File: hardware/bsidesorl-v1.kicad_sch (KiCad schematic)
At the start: 36 parts, among them J1 SAO Connector, U1 CH32V003F4P6, U2 TPS61023DRLR

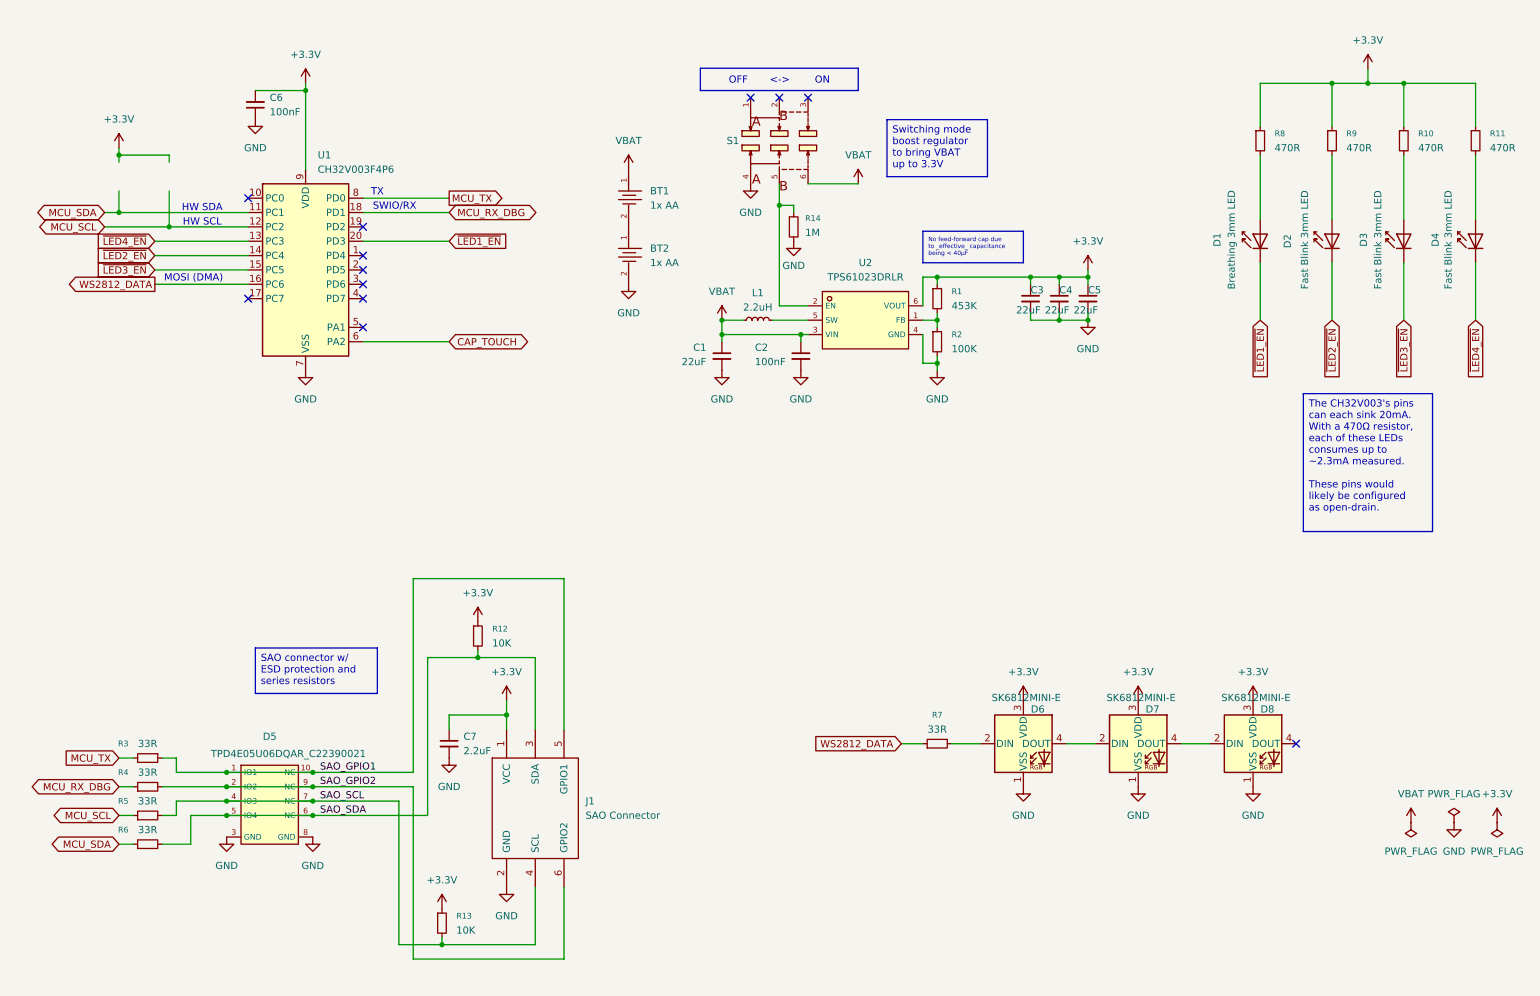
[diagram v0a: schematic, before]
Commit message: Final schematic, ready to order
* Switched from 2x AAs to 1x AAA
* Switched boost IC from TPS61023 to TPS61021A for lower VIN requirement due to single cell design change
* Added a second capacitive touch area just because
* Finalize back silkscreen
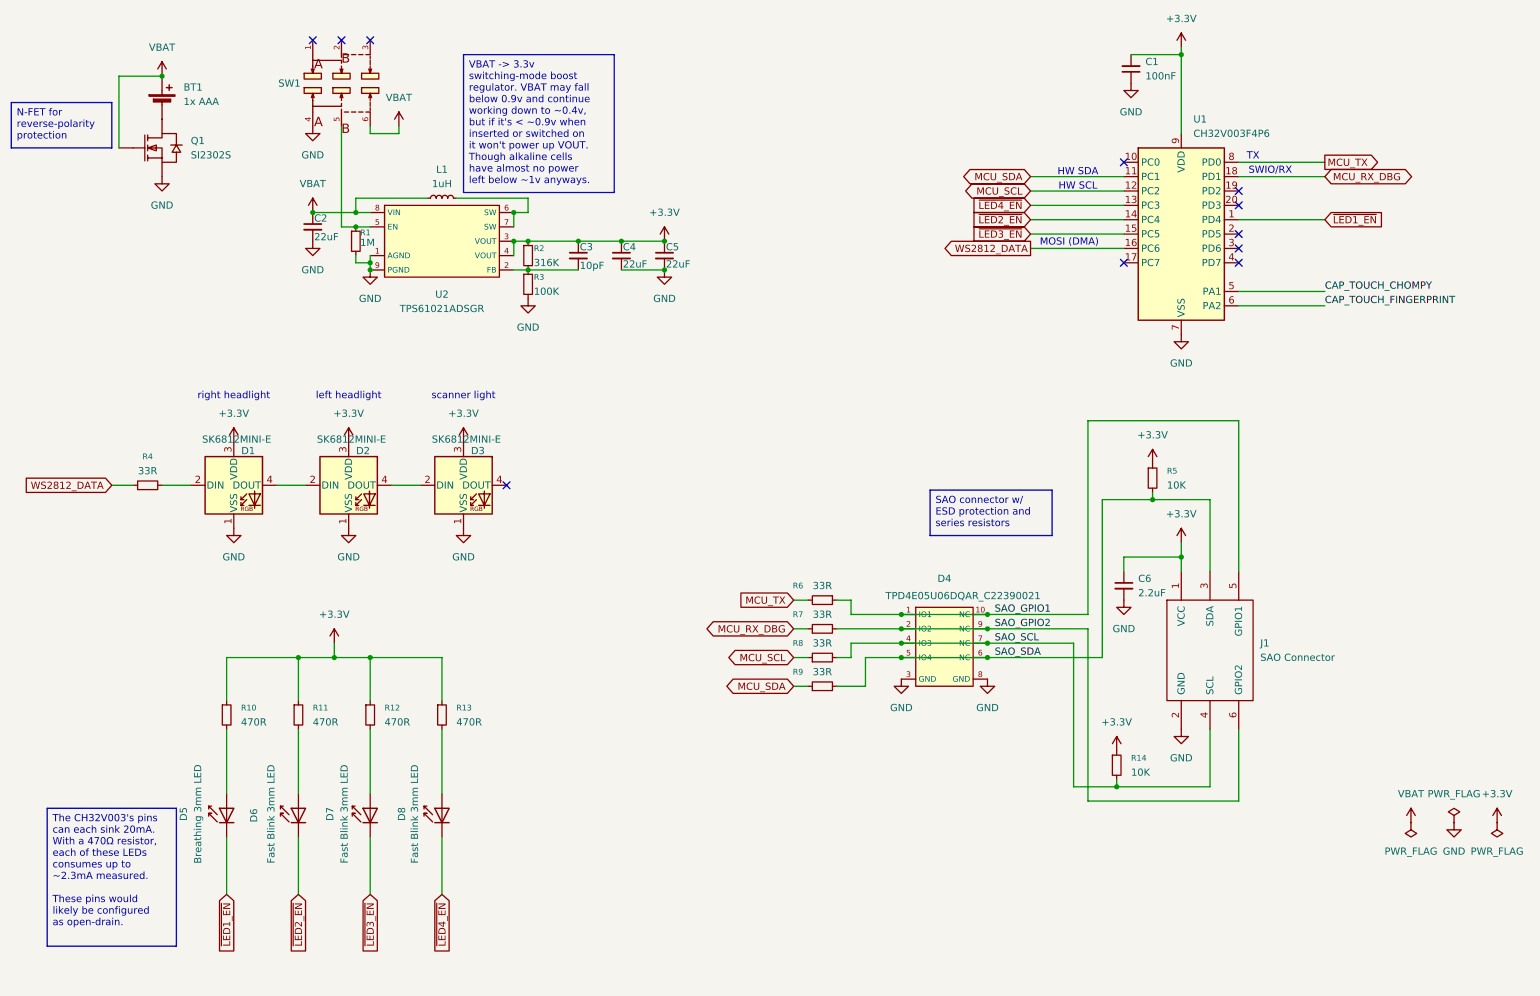
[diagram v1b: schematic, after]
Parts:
- removed BT1, BT2: 1x AA, footprint:BAT-TH_BH-AA-A5BJ012, symbol bsorl26:BH-AA-A5BJ012
- removed C1: 22uF, Capacitor_SMD:C_0603_1608Metric, symbol Device:C_Small
- removed R14: 1M, Resistor_SMD:R_0603_1608Metric, symbol Device:R_Small
- removed S1: MST22D18G2_125, footprint:SW-SMD_MST22D18G2, symbol bsorl26:MST22D18G2_125
- removed U2: TPS61023DRLR, footprint:SOT-563_L1.6-W1.2-P0.50-LS1.6-BR, symbol bsorl26:TPS61023DRLR
- added BT1: 1x AAA, footprint:BAT-TH_BH-AAA-1X, symbol Device:Battery_Cell
- added Q1: SI2302S, footprint:SOT-23-3_L2.9-W1.3-P1.90-LS2.4-BR, symbol bsorl26:SI2302S_C22463594
- added R3: 100K, Resistor_SMD:R_0603_1608Metric, symbol Device:R_Small
- added SW1: MST22D18G2_125, footprint:SW-SMD_MST22D18G2, symbol bsorl26:MST22D18G2_125
- added U2: TPS61021ADSGR, footprint:WSON-8_L2.0-W2.0-P0.50-TL-EP, symbol bsorl26:TPS61021ADSGR
- C2: value 100nF -> 22uF
- C3: value 22uF -> 10pF; LCSC C19702 -> (none)
- C4, C5: LCSC C19702 -> (none)
- L1: value 2.2uH -> 1uH; footprint footprint:IND-SMD_L3.5-W3.0 -> Inductor_SMD:L_1008_2520Metric; KiLib_Generator (none) -> SMD_2terminal_chip_molded
- R1: value 453K -> 1M; LCSC C25818 -> (none)
- R2: value 100K -> 316K; LCSC C25803 -> (none)
- renumbered C6 to C1, C7 to C6, D6 to D1, D7 to D2, D8 to D3, D5 to D4, D1 to D5, D2 to D6, D3 to D7, D4 to D8, R8 to R10, R9 to R11, R10 to R12, R11 to R13, R13 to R14, R7 to R4, R12 to R5, R3 to R6, R4 to R7, R5 to R8, R6 to R9
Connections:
- net +3.3V: now also R2.1, U2.3 (VOUT), U2.4 (VOUT); no longer R1.1
- net GND: now also R1.2, Q1.2 (S), R3.2, SW1.4, U2.1 (AGND), U2.9 (PGND); no longer C3.2, R2.2
- net VBAT: now also BT1.1 (+), Q1.1 (G), SW1.6, U2.8 (VIN)
- net ~{LED1_EN}: now also U1.1 (PD4); no longer U1.20 (PD3)
- net at L1.2: now also U2.6 (SW), U2.7 (SW)
- net CAP_TOUCH_CHOMPY: now reaches U1.5 (PA1)
- net CAP_TOUCH renamed CAP_TOUCH_FINGERPRINT
- new net: BT1.2 (-), Q1.3 (D)
- new net: R1.1, SW1.5, U2.5 (EN)
- new net: C3.2, R2.2, R3.1, U2.2 (FB)
- no-connect marks 12 -> 11
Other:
- note added: "left headlight"
- note added: "right headlight"
- note added: "scanner light"
- company: (none) -> Kevin Colley
- moved on the sheet: C1, C6, D1, D2, D3, D4, D5, D6, D7, D8, J1, R10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
